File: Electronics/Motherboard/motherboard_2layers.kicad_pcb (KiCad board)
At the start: 2 copper layers, 113.4 x 56 mm, 57 parts, among them J1 DX07S024JJ3R1300, J2 Conn_02x10_Odd_Even, M1 AO3400A, M2 AO3400A, M3 AO3400A, U1 AMS1117-3.3, U2 TMC2209_SILENTSTEPSTICK, U3 TMC2209_SILENTSTEPSTICK, U4 TMC2209_SILENTSTEPSTICK, U5 TMC2209_SILENTSTEPSTICK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

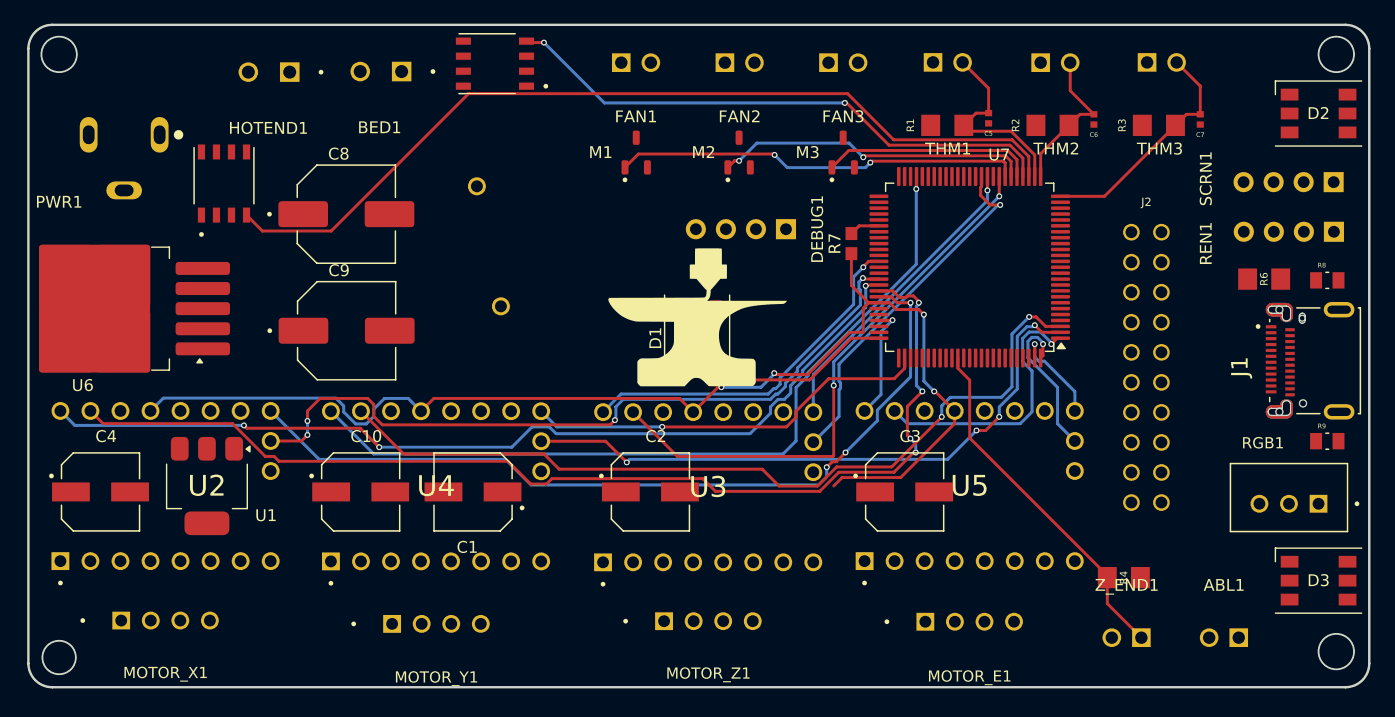
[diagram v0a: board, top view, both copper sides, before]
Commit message: fully finished data, partially finished power
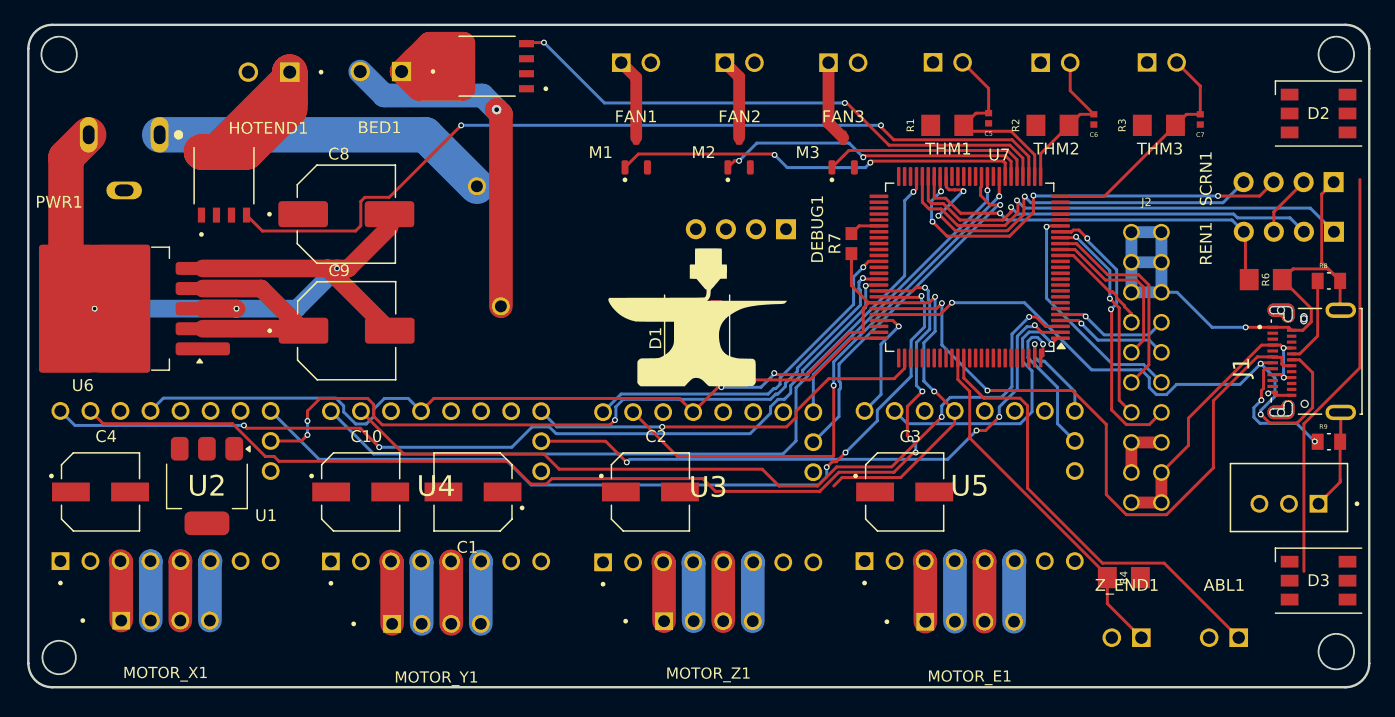
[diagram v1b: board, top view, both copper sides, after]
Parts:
- moved Q2 0.21 mm to (139.9, 75.5)
- moved J1 0.14 mm to (208.3, 100.5)
- moved R6 0.14 mm to (205.0, 93.5)
- moved R8 0.14 mm to (210.4, 93.7)
- moved R9 0.14 mm to (210.4, 107.3)
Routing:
- net GNDREF: track 0.00 -> 127.7 mm, vias 0 -> 5
- net USB_DM: track 0.00 -> 57.5 mm, vias 0 -> 2
- net USB_DP: track 0.00 -> 54.5 mm, vias 0 -> 3
- net +5V: track 0.00 -> 45.8 mm, vias 0 -> 2
- net EN_FOR: track 0.00 -> 40.5 mm, vias 0 -> 1
- net ABL: track 0.00 -> 38.1 mm
- net SCRN_SCL: track 0.00 -> 36.3 mm, vias 0 -> 4
- net EN_REV: track 0.00 -> 36.0 mm, vias 0 -> 1
- net Net-(D2-DOUT): track 0.00 -> 35.1 mm
- net SCRN_SDA: track 0.00 -> 34.8 mm, vias 0 -> 3
- net Net-(HOTEND1-Pad01): track 0.00 -> 34.4 mm
- net EN_BTN: track 0.00 -> 33.3 mm, vias 0 -> 1
- net VCC: track 0.00 -> 29.7 mm, vias 0 -> 1
- net Net-(F1-Pad1): track 0.00 -> 28.6 mm
- net Net-(BED1-Pad01): track 0.00 -> 26.8 mm
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
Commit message: 44 unrouted to go!!!
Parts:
- moved C4 0.31 mm to (106.8, 111.5), turned to 180 degrees
- moved MOTOR_X1 0.31 mm to (112.3, 122.9)
- moved U1 0.31 mm to (115.8, 111.0)
- moved U2 0.31 mm to (112.3, 111.0)
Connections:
- Q1 pad 1: unconnected-(Q1-S-Pad1) -> GNDREF
- Q1 pad 2: unconnected-(Q1-S-Pad2) -> GNDREF
- Q1 pad 3: unconnected-(Q1-S-Pad3) -> GNDREF
- Q2 pad 1: unconnected-(Q2-S-Pad1) -> GNDREF
- Q2 pad 2: unconnected-(Q2-S-Pad2) -> GNDREF
- Q2 pad 3: unconnected-(Q2-S-Pad3) -> GNDREF
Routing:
- net VCC: track 29.7 -> 273.2 mm, vias 1 -> 11
- net GNDREF: track 127.7 -> 320.0 mm, vias 5 -> 8
- net +3V3: track 10.3 -> 133.4 mm, vias 0 -> 3
- net +5V: track 45.8 -> 76.4 mm, vias 2 -> 5
- net DIAG_M1: track 63.0 -> 57.1 mm
- net EN_M1: track 72.6 -> 77.2 mm
- net DIAG_M3: track 52.8 -> 56.0 mm
- net STEP_M3: track 71.2 -> 72.9 mm
- net DIR_M3: track 67.9 -> 69.3 mm
- net HOTEND: track 74.6 -> 75.9 mm
- net BED: track 47.7 -> 48.8 mm
- net STEP_M1: track 94.0 -> 94.9 mm
- net DIR_M1: track 78.6 -> 79.3 mm

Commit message: yay finished
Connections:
- U7 pad 2: DIAG_M3 -> unconnected-(U7-PC10-Pad2)
- U7 pad 21: unconnected-(U7-PC0-Pad21) -> EN_BTN
- U7 pad 22: unconnected-(U7-PC1-Pad22) -> EN_REV
- U7 pad 23: unconnected-(U7-PC2-Pad23) -> EN_FOR
- U7 pad 3: STEP_M3 -> unconnected-(U7-PC11-Pad3)
- U7 pad 33: STEP_M2 -> unconnected-(U7-PC4-Pad33)
- U7 pad 44: EN_BTN -> unconnected-(U7-PE11-Pad44)
- U7 pad 45: EN_REV -> unconnected-(U7-PE12-Pad45)
- U7 pad 46: EN_FOR -> unconnected-(U7-PE13-Pad46)
- U7 pad 67: STEP_M1 -> unconnected-(U7-PD14-Pad67)
- U7 pad 68: EN_M1 -> unconnected-(U7-PD15-Pad68)
- U7 pad 72: DIR_M4 -> unconnected-(U7-PF8-Pad72)
- U7 pad 76: unconnected-(U7-PC8-Pad76) -> DIR_M4
- U7 pad 78: unconnected-(U7-PD0-Pad78) -> EN_M1
- U7 pad 79: unconnected-(U7-PD1-Pad79) -> STEP_M1
- U7 pad 95: unconnected-(U7-PE1-Pad95) -> STEP_M3
- U7 pad 96: unconnected-(U7-PE2-Pad96) -> DIAG_M3
- U7 pad 97: unconnected-(U7-PE3-Pad97) -> STEP_M2
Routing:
- net GNDREF: track 320.0 -> 566.0 mm, vias 8 -> 14
- net +5V: track 76.4 -> 244.9 mm, vias 5 -> 12
- net +3V3: track 133.4 -> 279.2 mm, vias 3 -> 9
- net Net-(D1-DOUT): track 0.00 -> 71.2 mm, vias 0 -> 4
- net SWCLK: track 0.00 -> 23.8 mm, vias 0 -> 3
- net SWDIO: track 0.00 -> 17.9 mm, vias 0 -> 2
- net EN_FOR: track 40.5 -> 24.1 mm
- net EN_REV: track 36.0 -> 21.4 mm
- net UART_RX: track 105.4 -> 91.2 mm
- net EN_BTN: track 33.3 -> 20.3 mm
- net USB_DM: track 57.5 -> 44.8 mm, vias 2 -> 4
- net STEP_M1: track 94.9 -> 83.6 mm, vias 4 -> 2
- net Net-(D2-DOUT): track 35.1 -> 46.4 mm
- net EN_M1: track 77.2 -> 67.7 mm
- net STEP_M3: track 72.9 -> 65.9 mm
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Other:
- copper layers 2 -> 4

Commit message: tiny bit of routing, more needs to be done
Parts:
- removed DEBUG1: Conn_01x04_Pin, PinHeader:PinHeader_1x04_P2.54mm_Vertical
- removed U7: STM32G0B1VETx, Package_QFP:LQFP-100_14x14mm_P0.5mm
- added U8: STM32F405RGTx, Package_QFP:LQFP-64_10x10mm_P0.5mm, F.Cu at (181.8, 92.3)
- moved R7 3.60 mm to (173.5, 91.3)
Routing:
- net +3V3: track 279.2 -> 239.3 mm, vias 9 -> 7
- net SCRN_SCL: track 33.3 -> 5.19 mm, vias 2 -> 1
- net SCRN_SDA: track 29.9 -> 2.47 mm, vias 1 -> 0
- net GNDREF: track 566.0 -> 541.0 mm, vias 14 -> 12
- net SWCLK: track 23.8 -> 0.00 mm, vias 3 -> 0
- net EN_M2: track 26.0 -> 3.16 mm, vias 1 -> 0
- net DIAG_M2: track 30.4 -> 7.64 mm, vias 1 -> 0
- net UART_RX: track 91.2 -> 69.1 mm, vias 4 -> 3
- net STEP_M2: track 47.9 -> 26.4 mm, vias 2 -> 1
- net Net-(D1-DOUT): track 71.2 -> 52.7 mm, vias 4 -> 2
- net SWDIO: track 17.9 -> 0.00 mm, vias 2 -> 0
- net USB_DM: track 44.8 -> 35.3 mm, vias 4 -> 2
- net DIR_M3: track 69.3 -> 60.5 mm, vias 1 -> 0
- net PF5: track 19.9 -> 12.7 mm, vias 1 -> 0
- net EN_M1: track 67.7 -> 60.9 mm, vias 3 -> 1
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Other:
- copper layers 4 -> 2

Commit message: moar routing
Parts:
- moved R7 3.68 mm to (173.0, 95.0)
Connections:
- U8 pad 10: unconnected-(U8-PC2-Pad10) -> UART_TX
- U8 pad 11: unconnected-(U8-PC3-Pad11) -> DIR_M2
- U8 pad 14: unconnected-(U8-PA0-Pad14) -> DIAG_M1
- U8 pad 15: unconnected-(U8-PA1-Pad15) -> DIR_M1
- U8 pad 16: unconnected-(U8-PA2-Pad16) -> DIR_M3
- U8 pad 17: unconnected-(U8-PA3-Pad17) -> NEOPIXEL_DIN
- U8 pad 20: unconnected-(U8-PA4-Pad20) -> EN_M3
- U8 pad 21: unconnected-(U8-PA5-Pad21) -> DIR_M4
- U8 pad 5: unconnected-(U8-PH0-Pad5) -> STEP_M2
- U8 pad 6: unconnected-(U8-PH1-Pad6) -> DIAG_M2
- U8 pad 8: unconnected-(U8-PC0-Pad8) -> EN_M2
- U8 pad 9: unconnected-(U8-PC1-Pad9) -> UART_RX
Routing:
- net GNDREF: track 541.0 -> 567.3 mm, vias 12 -> 17
- net UART_RX: track 69.1 -> 90.3 mm, vias 3 -> 4
- net Net-(D1-DOUT): track 52.7 -> 70.4 mm, vias 2 -> 4
- net +3V3: track 239.3 -> 255.2 mm, vias 7 -> 8
- net EN_M2: track 3.16 -> 18.5 mm, vias 0 -> 1
- net EN_M1: track 60.9 -> 76.1 mm
- net STEP_M2: track 26.4 -> 41.5 mm, vias 1 -> 2
- net DIAG_M2: track 7.64 -> 22.2 mm, vias 0 -> 1
- net DIR_M4: track 3.73 -> 13.3 mm
- net EN_M3: track 32.5 -> 41.0 mm
- net NEOPIXEL_DIN: track 17.5 -> 24.8 mm
- net DIR_M1: track 76.4 -> 81.4 mm, vias 2 -> 3
- net UART_TX: track 0.00 -> 4.02 mm
- net T0: track 20.3 -> 23.5 mm
- net DIAG_M1: track 58.8 -> 62.0 mm
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
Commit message: its almost dne, need to do zone fill
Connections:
- J2 pad 10: PF2 -> PB14
- J2 pad 11: PE4 -> PC8
- J2 pad 12: PF1 -> PC7
- J2 pad 13: PE5 -> PC9
- J2 pad 14: PF0 -> PC6
- J2 pad 7: PF4 -> PB13
- J2 pad 8: PF3 -> PB12
- J2 pad 9: PF5 -> PB15
- U8 pad 33: unconnected-(U8-PB12-Pad33) -> PB12
- U8 pad 34: unconnected-(U8-PB13-Pad34) -> PB13
- U8 pad 35: unconnected-(U8-PB14-Pad35) -> PB14
- U8 pad 36: unconnected-(U8-PB15-Pad36) -> PB15
- U8 pad 37: unconnected-(U8-PC6-Pad37) -> PC6
- U8 pad 38: unconnected-(U8-PC7-Pad38) -> PC7
- U8 pad 39: unconnected-(U8-PC8-Pad39) -> PC8
- U8 pad 40: unconnected-(U8-PC9-Pad40) -> PC9
- U8 pad 41: unconnected-(U8-PA8-Pad41) -> EN_FOR
- U8 pad 42: unconnected-(U8-PA9-Pad42) -> EN_REV
- U8 pad 43: unconnected-(U8-PA10-Pad43) -> EN_BTN
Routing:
- net SCRN_SDA: track 2.47 -> 25.6 mm, vias 0 -> 1
- net SCRN_SCL: track 5.19 -> 26.8 mm, vias 1 -> 2
- net PF4: track 20.9 -> 0.00 mm, vias 2 -> 0
- net PF3: track 16.8 -> 0.00 mm, vias 1 -> 0
- net PB13: track 0.00 -> 15.0 mm
- net PB15: track 0.00 -> 14.4 mm
- net PC9: track 0.00 -> 13.9 mm
- net PC8: track 0.00 -> 13.9 mm
- net PF2: track 12.7 -> 0.00 mm
- net PF5: track 12.7 -> 0.00 mm
- net PC7: track 0.00 -> 12.3 mm
- net PB14: track 0.00 -> 11.7 mm
- net PB12: track 0.00 -> 11.3 mm
- net PF1: track 9.41 -> 0.00 mm
- net PE4: track 7.78 -> 0.00 mm, vias 1 -> 0
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
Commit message: yessir we finished!!! can someone check this over???
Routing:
- net GNDREF: track 563.8 -> 397.5 mm, vias 16 -> 9
- net UART_RX: track 90.3 -> 96.4 mm, vias 4 -> 5
- net +5V: track 245.0 -> 241.5 mm, vias 12 -> 14
- net Net-(D2-DOUT): track 46.4 -> 49.2 mm, vias 0 -> 2
- net PC9: track 13.9 -> 11.7 mm, vias 0 -> 1
- net PC7: track 12.3 -> 10.7 mm, vias 0 -> 1
- net Net-(D1-DOUT): track 70.6 -> 69.6 mm
- net PC8: track 13.9 -> 13.0 mm
- net +3V3: track 261.6 -> 261.7 mm, vias 8 -> 12
- added copper zone on F.Cu, net GNDREF

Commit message: updated schmentic with proper values and updated usb c connector
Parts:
- removed J1: DX07S024JJ3R1300, DX07S024JJ3R1300:JAE_DX07S024JJ3R1300
- added USB_C1: TYPE-C-31-M-12, Connector_USB:USB_C_Receptacle_HRO_TYPE-C-31-M-12, F.Cu at (209.8, 100.5)
- C1, C2, C3, C4: value EEEFT1V101AP -> 100uf 35v
- C10: value EEEFN1C221XP -> 220uf 16v
- C8: value UWT1V101MCL1GS -> 100uf 35v
- C9: value UWT1V331MNL1GS -> 330uf 35v
- FAN1: value B2B-XH-A -> ~
- R4, R6: value RC1206JR-134K7L -> 4.7k
- R7: value RC0603FR-131KL -> 1k
- R8, R9: value RMCF0805JT5K10 -> 5.1k
- renumbered U2 to S1, U4 to S2, U3 to S3, U5 to S4
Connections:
- MOTOR_E1 pad 1: Net-(U5-M1B) -> Net-(S4-M1B)
- MOTOR_E1 pad 2: Net-(U5-M1A) -> Net-(S4-M1A)
- MOTOR_E1 pad 3: Net-(U5-M2A) -> Net-(S4-M2A)
- MOTOR_E1 pad 4: Net-(U5-M2B) -> Net-(S4-M2B)
- MOTOR_X1 pad 1: Net-(U2-M1B) -> Net-(S1-M1B)
- MOTOR_X1 pad 2: Net-(U2-M1A) -> Net-(S1-M1A)
- MOTOR_X1 pad 3: Net-(U2-M2A) -> Net-(S1-M2A)
- MOTOR_X1 pad 4: Net-(U2-M2B) -> Net-(S1-M2B)
- MOTOR_Y1 pad 1: Net-(U4-M1B) -> Net-(S2-M1B)
- MOTOR_Y1 pad 2: Net-(U4-M1A) -> Net-(S2-M1A)
- MOTOR_Y1 pad 3: Net-(U4-M2A) -> Net-(S2-M2A)
- MOTOR_Y1 pad 4: Net-(U4-M2B) -> Net-(S2-M2B)
- MOTOR_Z1 pad 1: Net-(U3-M1B) -> Net-(S3-M1B)
- MOTOR_Z1 pad 2: Net-(U3-M1A) -> Net-(S3-M1A)
- MOTOR_Z1 pad 3: Net-(U3-M2A) -> Net-(S3-M2A)
- MOTOR_Z1 pad 4: Net-(U3-M2B) -> Net-(S3-M2B)
- Q1 pad 1: GNDREF -> unconnected-(Q1-S-Pad1)
- Q1 pad 2: GNDREF -> unconnected-(Q1-S-Pad2)
- Q1 pad 3: GNDREF -> unconnected-(Q1-S-Pad3)
- Q2 pad 1: GNDREF -> unconnected-(Q2-S-Pad1)
- Q2 pad 2: GNDREF -> unconnected-(Q2-S-Pad2)
- Q2 pad 3: GNDREF -> unconnected-(Q2-S-Pad3)
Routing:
- net GNDREF: track 397.5 -> 0.00 mm, vias 9 -> 0
- net Net-(BED1-Pad01): track 26.8 -> 0.00 mm
- net VCC: track 273.2 -> 257.5 mm, vias 11 -> 10
- net HOTEND: track 75.4 -> 69.7 mm
- net STEP_M3: track 68.5 -> 66.7 mm
- net DIAG_M3: track 56.1 -> 54.7 mm
- net STEP_M4: track 21.5 -> 20.2 mm
- added copper zone on F.Cu, net Net-(BED1-Pad01)
